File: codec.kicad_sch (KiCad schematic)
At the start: 30 parts, among them J10 FCR684204T, J11 DIN_DOUT_2TP, J13 AJ_TP5, J14 C_G0, J15 C_G7, J16 CRST, J17 C_CLKOUT, J3 Conn_01x02_Pin, U4 WM8805GEDS_V, Y2 12M

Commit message: rework the atmega168 reset signal schematics and routing
Signed-off-by: Mika Laitio <lamikr@gmail.com>
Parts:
- R14: footprint Resistor_SMD:R_0402_1005Metric -> Resistor_SMD:R_0603_1608Metric
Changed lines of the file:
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@@
 			)
 		)
-		(property "Footprint" "Resistor_SMD:R_0402_1005Metric"
+		(property "Footprint" "Resistor_SMD:R_0603_1608Metric"
 			(at 194.31 151.638 90)
 			(effects

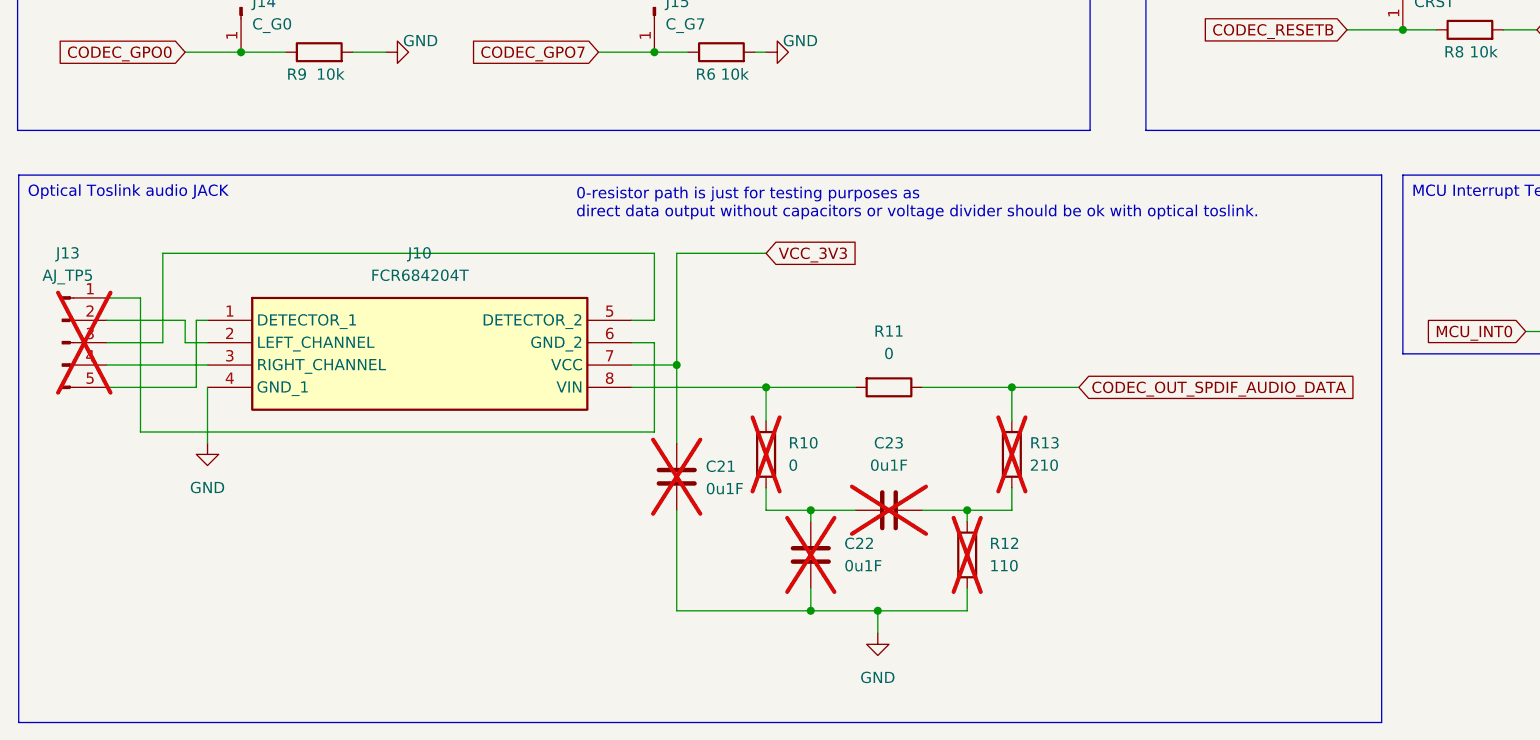
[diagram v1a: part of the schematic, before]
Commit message: fix toslink pin6 grounding
- had problem already on v1 boards
- move toslink/3.5mm plug little out of board
- re-arrange alternative output

Signed-off-by: Mika Laitio <lamikr@gmail.com>
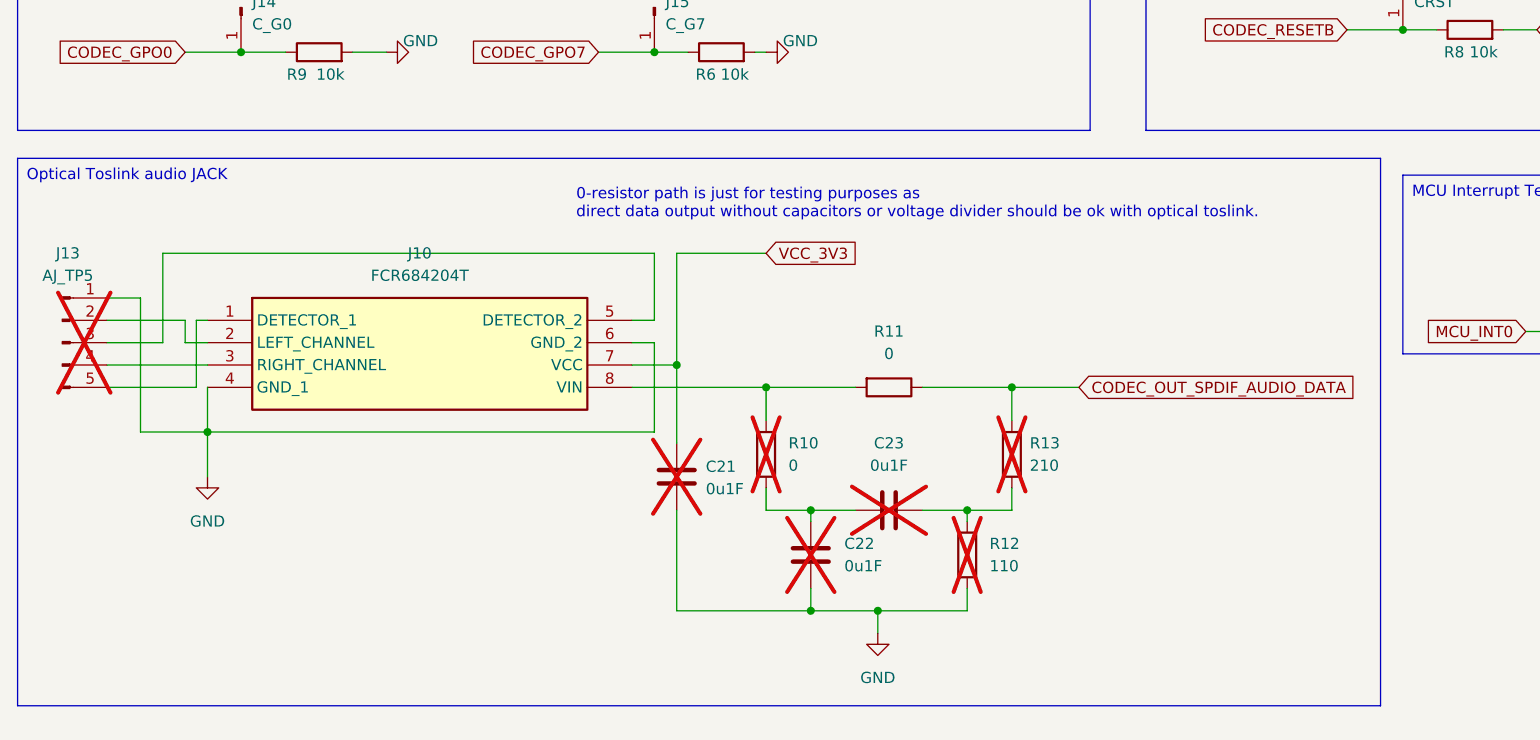
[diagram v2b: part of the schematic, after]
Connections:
- net GND: now also J10.6 (GND_2), J13.1 (Pin_1)
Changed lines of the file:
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@@
+	)
+	(junction
+		(at 38.1 161.29)
+		(diameter 0)
+		(color 0 0 0 0)
 	)
 	(junction
@@
 	(wire
 		(pts
+			(xy 30.48 161.29) (xy 38.1 161.29)
+		)
+		(stroke
+			(width 0)
+			(type default)
+		)
+	)
+	(wire
+		(pts
 			(xy 124.46 171.45) (xy 124.46 170.18)
 		)
@@
 	(wire
 		(pts
+			(xy 38.1 161.29) (xy 88.9 161.29)
+		)
+		(stroke
+			(width 0)
+			(type default)
+		)
+	)
+	(wire
+		(pts
 			(xy 60.96 38.1) (xy 67.31 38.1)
 		)
@@
 	(wire
 		(pts
-			(xy 30.48 161.29) (xy 88.9 161.29)
-		)
-		(stroke
-			(width 0)
-			(type default)
-		)
-	)
-	(wire
-		(pts
 			(xy 133.35 43.18) (xy 133.35 45.72)
 		)
@@
 	(wire
 		(pts
+			(xy 38.1 161.29) (xy 38.1 166.37)
+		)
+		(stroke
+			(width 0)
+			(type default)
+		)
+	)
+	(wire
+		(pts
 			(xy 26.67 153.67) (xy 38.1 153.67)
 		)
@@
 	(wire
 		(pts
-			(xy 38.1 156.21) (xy 38.1 162.56)
+			(xy 38.1 156.21) (xy 38.1 161.29)
 		)
 		(stroke
@@
 	(text_box "Optical Toslink audio JACK"
 		(exclude_from_sim no)
-		(at 16.637 132.08 0)
+		(at 16.51 130.175 0)
 		(size 154.94 62.23)
 		(stroke
@@
 	(symbol
 		(lib_id "power:GND")
-		(at 38.1 162.56 0)
+		(at 38.1 166.37 0)
 		(unit 1)
 		(exclude_from_sim no)
@@
 		(fields_autoplaced yes)
 		(property "Reference" "#PWR023"
-			(at 38.1 168.91 0)
+			(at 38.1 172.72 0)
 			(effects
 				(font
@@
 		)
 		(property "Value" "GND"
-			(at 38.1 167.64 0)
+			(at 38.1 171.45 0)
 			(effects
 				(font
@@
 		)
 		(property "Footprint" ""
-			(at 38.1 162.56 0)
+			(at 38.1 166.37 0)
 			(effects
 				(font
@@
 		)
 		(property "Datasheet" ""
-			(at 38.1 162.56 0)
+			(at 38.1 166.37 0)
 			(effects
 				(font
@@
 		)
 		(property "Description" "Power symbol creates a global label with name \"GND\" , ground"
-			(at 38.1 162.56 0)
-			(effects
-				(font
+			(at 38.1 166.37 0)
+			(effects
+				(font
